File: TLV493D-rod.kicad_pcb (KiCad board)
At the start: 2 copper layers, 100 x 7 mm, 9 parts, among them CN1 AFC10-S04QCA-00, J1 Conn_01x04_Pin, U1 TLV493D

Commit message: add branding
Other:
- board text added: "FTIndustries TLV493D"
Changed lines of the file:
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@@
     (effects (font (size 1 1) (thickness 0.15)) (justify left bottom mirror))
+  )
+  (gr_text "FTIndustries TLV493D" (at 194.4116 109.855) (layer "F.SilkS")
+    (effects (font (size 1 1) (thickness 0.15)) (justify left bottom))
   )
   (dimension (type aligned) (layer "Dwgs.User")

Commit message: fix incorrect footprint
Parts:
- U1: footprint Package_TO_SOT_SMD:SOT-23-6 -> TLV493D-rod:SOP-6_L3.0-W1.5-P0.95-LS2.5-BR
- turned U1 to 90 degrees
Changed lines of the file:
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@@
     (descr "Mounting Hole 2.2mm, no annular, M2")
     (tags "mounting hole 2.2mm no annular m2")
-    (attr exclude_from_pos_files exclude_from_bom)
+    (attr board_only exclude_from_pos_files exclude_from_bom)
     (fp_text reference "hole2" (at 0 -3.2) (layer "F.SilkS") hide
         (effects (font (size 1 1) (thickness 0.15)))
@@
     )
   )
-  (footprint "Package_TO_SOT_SMD:SOT-23-6" (layer "F.Cu")
-    (at 139.7 107.5 -90)
-    (descr "SOT, 6 Pin (https://www.jedec.org/sites/default/files/docs/Mo-178c.PDF variant AB), generated with kicad-footprint-generator ipc_gullwing_generator.py")
-    (tags "SOT TO_SOT_SMD")
+  (footprint "TLV493D-rod:SOP-6_L3.0-W1.5-P0.95-LS2.5-BR" (layer "F.Cu")
+    (at 139.7 107.5 90)
     (property "Sheetfile" "TLV493D-rod.kicad_sch")
     (property "Sheetname" "")
@@
     (property "ki_keywords" "magnetic field i2c")
     (attr smd)
-    (fp_text reference "U1" (at -3.175 0 90) (layer "F.SilkS") hide
-        (effects (font (size 1 1) (thickness 0.15)))
-    )
-    (fp_text value "TLV493D" (at 0 2.4 90) (layer "F.Fab")
-        (effects (font (size 1 1) (thickness 0.15)))
-    )
-    (fp_text user "${REFERENCE}" (at 0 0 90) (layer "F.Fab")
-        (effects (font (size 0.4 0.4) (thickness 0.06)))
-    )
-    (fp_line (start 0 -1.56) (end -1.8 -1.56)
-      (stroke (width 0.12) (type solid)) (layer "F.SilkS"))
-    (fp_line (start 0 -1.56) (end 0.8 -1.56)
-      (stroke (width 0.12) (type solid)) (layer "F.SilkS"))
-    (fp_line (start 0 1.56) (end -0.8 1.56)
-      (stroke (width 0.12) (type solid)) (layer "F.SilkS"))
-    (fp_line (start 0 1.56) (end 0.8 1.56)
-      (stroke (width 0.12) (type solid)) (layer "F.SilkS"))
-    (fp_line (start -2.05 -1.7) (end -2.05 1.7)
-      (stroke (width 0.05) (type solid)) (layer "F.CrtYd"))
-    (fp_line (start -2.05 1.7) (end 2.05 1.7)
-      (stroke (width 0.05) (type solid)) (layer "F.CrtYd"))
-    (fp_line (start 2.05 -1.7) (end -2.05 -1.7)
-      (stroke (width 0.05) (type solid)) (layer "F.CrtYd"))
-    (fp_line (start 2.05 1.7) (end 2.05 -1.7)
-      (stroke (width 0.05) (type solid)) (layer "F.CrtYd"))
-    (fp_line (start -0.8 -1.05) (end -0.4 -1.45)
-      (stroke (width 0.1) (type solid)) (layer "F.Fab"))
-    (fp_line (start -0.8 1.45) (end -0.8 -1.05)
-      (stroke (width 0.1) (type solid)) (layer "F.Fab"))
-    (fp_line (start -0.4 -1.45) (end 0.8 -1.45)
-      (stroke (width 0.1) (type solid)) (layer "F.Fab"))
-    (fp_line (start 0.8 -1.45) (end 0.8 1.45)
-      (stroke (width 0.1) (type solid)) (layer "F.Fab"))
-    (fp_line (start 0.8 1.45) (end -0.8 1.45)
-      (stroke (width 0.1) (type solid)) (layer "F.Fab"))
-    (pad "1" smd roundrect (at -1.1375 -0.95 270) (size 1.325 0.6) (layers "F.Cu" "F.Paste" "F.Mask") (roundrect_rratio 0.25)
+    (fp_text reference "U1" (at 0 -4.95 90) (layer "F.SilkS")
+        (effects (font (size 1 1) (thickness 0.15)))
+    )
+    (fp_text value "TLV493D" (at 0 4.95 90) (layer "F.Fab")
+        (effects (font (size 1 1) (thickness 0.15)))
+    )
+    (fp_text user "${REFERENCE}" (at 0 0 90) (layer "F.Fab")
+        (effects (font (size 1 1) (thickness 0.15)))
+    )
+    (fp_line (start -0.8 -1.5) (end 0.8 -1.5)
+      (stroke (width 0.2) (type solid)) (layer "F.SilkS"))
+    (fp_line (start -0.8 -1.45) (end -0.8 -1.5)
+      (stroke (width 0.2) (type solid)) (layer "F.SilkS"))
+    (fp_line (start -0.8 1.5) (end -0.8 1.45)
+      (stroke (width 0.2) (type solid)) (layer "F.SilkS"))
+    (fp_line (start 0.8 -1.5) (end 0.8 -1.45)
+      (stroke (width 0.2) (type solid)) (layer "F.SilkS"))
+    (fp_line (start 0.8 1.45) (end 0.8 1.5)
+      (stroke (width 0.2) (type solid)) (layer "F.SilkS"))
+    (fp_line (start 0.8 1.5) (end -0.8 1.5)
+      (stroke (width 0.2) (type solid)) (layer "F.SilkS"))
+    (fp_circle (center 1.3 1.6) (end 1.44 1.6)
+      (stroke (width 0.15) (type solid)) (fill none) (layer "F.SilkS"))
+    (fp_circle (center 2.04 0.93) (end 2.24 0.93)
+      (stroke (width 0.4) (type solid)) (fill none) (layer "Cmts.User"))
+    (fp_circle (center 1.25 1.5) (end 1.28 1.5)
+      (stroke (width 0.06) (type solid)) (fill none) (layer "F.Fab"))
+    (pad "1" smd rect (at 1.2 0.95 270) (size 1.3 0.55) (layers "F.Cu" "F.Paste" "F.Mask")
       (net 3 "/SCL") (pinfunction "SCL/INT") (pintype "bidirectional"))
-    (pad "2" smd roundrect (at -1.1375 0 270) (size 1.325 0.6) (layers "F.Cu" "F.Paste" "F.Mask") (roundrect_rratio 0.25)
+    (pad "2" smd rect (at 1.2 0 270) (size 1.3 0.55) (layers "F.Cu" "F.Paste" "F.Mask")
       (net 2 "GND") (pinfunction "GND") (pintype "power_in"))
-    (pad "3" smd roundrect (at -1.1375 0.95 270) (size 1.325 0.6) (layers "F.Cu" "F.Paste" "F.Mask") (roundrect_rratio 0.25)
+    (pad "3" smd rect (at 1.2 -0.95 270) (size 1.3 0.55) (layers "F.Cu" "F.Paste" "F.Mask")
       (net 2 "GND") (pinfunction "GND") (pintype "power_in"))
-    (pad "4" smd roundrect (at 1.1375 0.95 270) (size 1.325 0.6) (layers "F.Cu" "F.Paste" "F.Mask") (roundrect_rratio 0.25)
+    (pad "4" smd rect (at -1.19 -0.95 270) (size 1.3 0.55) (layers "F.Cu" "F.Paste" "F.Mask")
       (net 1 "+3V3") (pinfunction "VDD") (pintype "power_in"))
-    (pad "5" smd roundrect (at 1.1375 0 270) (size 1.325 0.6) (layers "F.Cu" "F.Paste" "F.Mask") (roundrect_rratio 0.25)
+    (pad "5" smd rect (at -1.2 0 270) (size 1.3 0.55) (layers "F.Cu" "F.Paste" "F.Mask")
       (net 2 "GND") (pinfunction "GND") (pintype "power_in"))
-    (pad "6" smd roundrect (at 1.1375 -0.95 270) (size 1.325 0.6) (layers "F.Cu" "F.Paste" "F.Mask") (roundrect_rratio 0.25)
+    (pad "6" smd rect (at -1.19 0.95 270) (size 1.3 0.55) (layers "F.Cu" "F.Paste" "F.Mask")
       (net 4 "/SDA") (pinfunction "SDA/ADDR") (pintype "bidirectional"))
-    (model "${KICAD6_3DMODEL_DIR}/Package_TO_SOT_SMD.3dshapes/SOT-23-6.wrl"
-      (offset (xyz 0 0 0))
-      (scale (xyz 1 1 1))
-      (rotate (xyz 0 0 0))
+    (model "C:/Users/wb/Documents/electronics/TLV493D-rod/lib/TLV493D-rod.3dshapes/TSOP-6_L3.0-W1.5-H1.0-LS2.8-P0.95.wrl"
+      (offset (xyz 0 -0 -0))
+      (scale (xyz 1 1 1))
+      (rotate (xyz 0 0 180))
     )
   )
@@
     (descr "Mounting Hole 2.2mm, no annular, M2")
     (tags "mounting hole 2.2mm no annular m2")
-    (attr exclude_from_pos_files exclude_from_bom)
+    (attr board_only exclude_from_pos_files exclude_from_bom)
     (fp_text reference "hole1" (at 0 -3.2) (layer "F.SilkS") hide
         (effects (font (size 1 1) (thickness 0.15)))

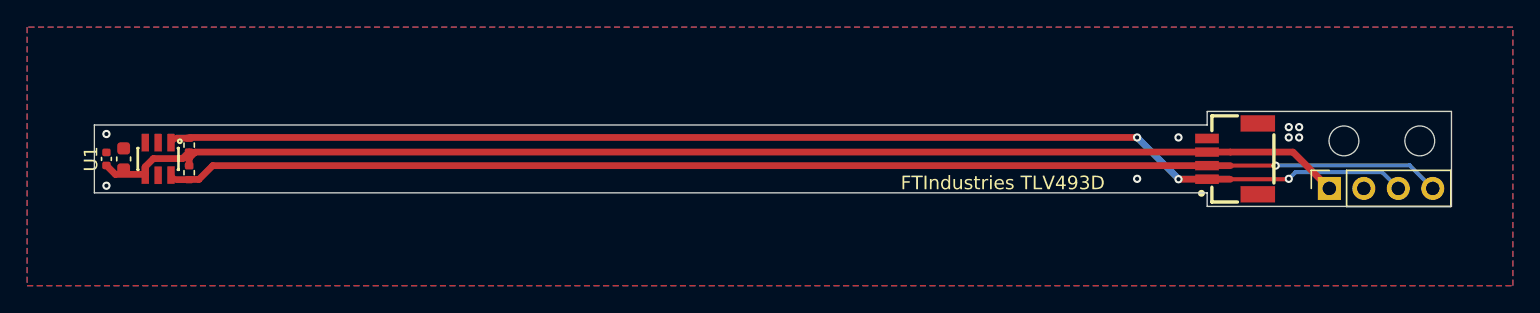
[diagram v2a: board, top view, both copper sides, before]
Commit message: revamp mounting, fix qwiic pinout
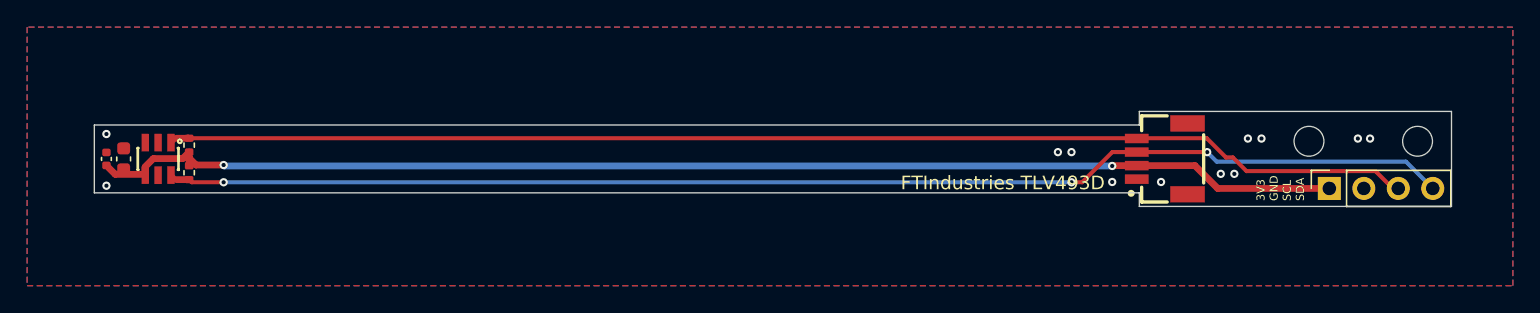
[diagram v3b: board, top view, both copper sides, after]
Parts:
- removed hole1, hole2: MountingHole_2.2mm_M2, MountingHole:MountingHole_2.2mm_M2
- added H1: MountingHole, MountingHole:MountingHole_2.2mm_M2, F.Cu at (224.5, 106.2)
- added H2: MountingHole, MountingHole:MountingHole_2.2mm_M2, F.Cu at (232.5, 106.2)
- moved CN1 5.18 mm to (213.7, 107.5)
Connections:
- CN1 pad 1: /SCL -> GND
- CN1 pad 2: /SDA -> +3V3
- CN1 pad 3: +3V3 -> /SDA
- CN1 pad 4: GND -> /SCL
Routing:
- net /SDA: track 94.3 -> 95.3 mm, vias 1 -> 3
- net /SCL: track 92.6 -> 92.2 mm, vias 3 -> 0
- net +3V3: track 93.7 -> 93.3 mm, vias 0 -> 2
- net GND: vias 8 -> 12
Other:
- outline, holes or cut-outs redrawn
- board text added: "3V3 GND SCL SDA"
